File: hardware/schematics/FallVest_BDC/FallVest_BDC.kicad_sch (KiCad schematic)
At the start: 6 parts, among them Q1 AO3400A, U2 ESP32-WROOM-32, U3 4554, U4 NEO-6M

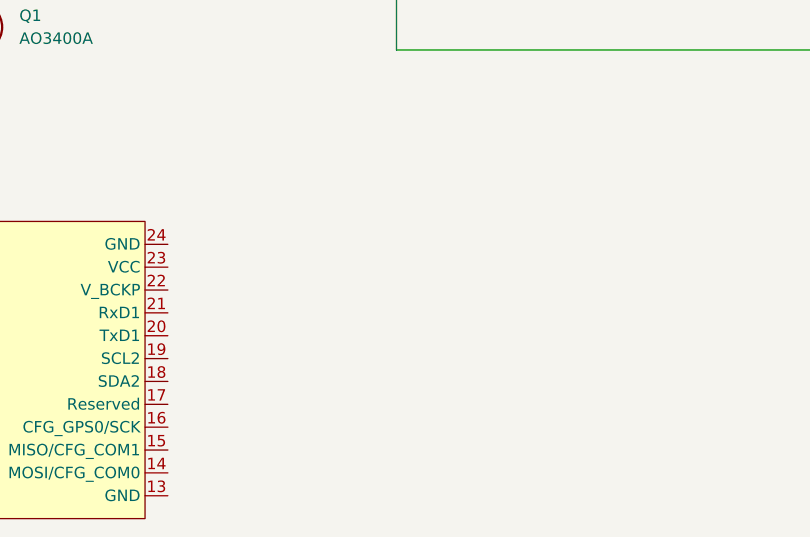
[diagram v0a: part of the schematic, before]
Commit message: Magnetometer
Added ICM-20948
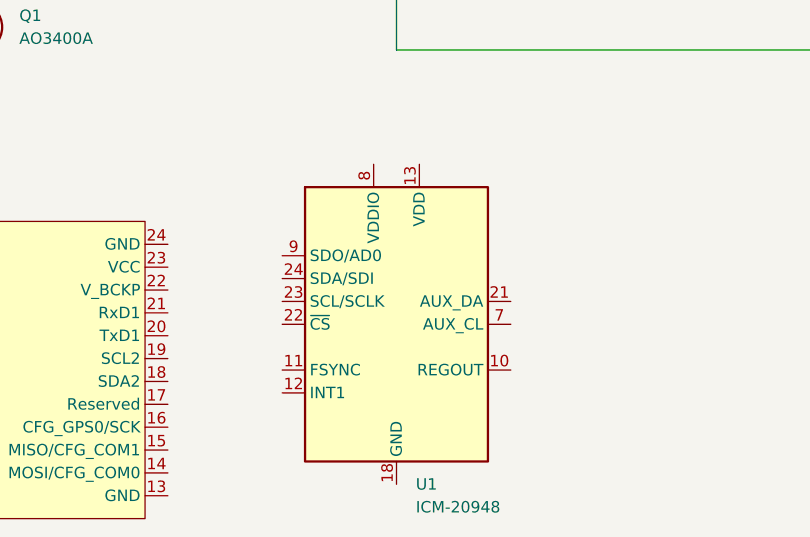
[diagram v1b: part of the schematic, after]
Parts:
- added U1: ICM-20948, Sensor_Motion:InvenSense_QFN-24_3x3mm_P0.4mm, symbol Sensor_Motion:ICM-20948
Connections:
- new net: U1.18 (GND), U1.20 (GND)
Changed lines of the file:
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@@
+	)
+	(symbol
+		(lib_id "Sensor_Motion:ICM-20948")
+		(at 88.9 168.91 0)
+		(unit 1)
+		(exclude_from_sim no)
+		(in_bom yes)
+		(on_board yes)
+		(dnp no)
+		(fields_autoplaced yes)
+		(property "Reference" "U1"
+			(at 91.0433 186.69 0)
+			(effects
+				(font
+					(size 1.27 1.27)
+				)
+				(justify left)
+			)
+		)
+		(property "Value" "ICM-20948"
+			(at 91.0433 189.23 0)
+			(effects
+				(font
+					(size 1.27 1.27)
+				)
+				(justify left)
+			)
+		)
+		(property "Footprint" "Sensor_Motion:InvenSense_QFN-24_3x3mm_P0.4mm"
+			(at 88.9 194.31 0)
+			(effects
+				(font
+					(size 1.27 1.27)
+				)
+				(hide yes)
+			)
+		)
+		(property "Datasheet" "http://www.invensense.com/wp-content/uploads/2016/06/DS-000189-ICM-20948-v1.3.pdf"
+			(at 88.9 172.72 0)
+			(effects
+				(font
+					(size 1.27 1.27)
+				)
+				(hide yes)
+			)
+		)
+		(property "Description" "InvenSense 9-Axis Motion Sensor, Accelerometer, Gyroscope, Compass, I2C/SPI, QFN-24"
+			(at 88.9 168.91 0)
+			(effects
+				(font
+					(size 1.27 1.27)
+				)
+				(hide yes)
+			)
+		)
+		(pin "13"
+		)
+		(pin "11"
+		)
+		(pin "20"
+		)
+		(pin "22"
+		)
+		(pin "9"
+		)
+		(pin "8"
+		)
+		(pin "6"
+		)
+		(pin "4"
+		)
+		(pin "1"
+		)
+		(pin "3"
+		)
+		(pin "2"
+		)
+		(pin "23"
+		)
+		(pin "12"
+		)
+		(pin "18"
+		)
+		(pin "5"
+		)
+		(pin "14"
+		)
+		(pin "15"
+		)
+		(pin "7"
+		)
+		(pin "10"
+		)
+		(pin "17"
+		)
+		(pin "24"
+		)
+		(pin "21"
+		)
+		(pin "16"
+		)
+		(pin "19"
+		)
+		(instances
+			(project ""
+				(path "/74063a4b-f2d6-40f5-8694-30dc3de3f53f"
+					(reference "U1")
+					(unit 1)
+				)
+			)
+		)
 	)
 	(symbol

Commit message: Update
Some minor tweaking.
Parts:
- removed U1: ICM-20948, Sensor_Motion:InvenSense_QFN-24_3x3mm_P0.4mm, symbol Sensor_Motion:ICM-20948
- added D1: SS34, Diode_SMD:D_SMA, symbol Diode:SS34
- added R: 220, symbol Device:R_US
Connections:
- net GND: now also Q1.2 (S), U2.1 (GND), U2.15 (GND), U2.38 (GND), U2.39 (GND); no longer U3.JP3_2 (SDO/ADR)
- net at Q1.1 (G): now also Q1.3 (D), D1.2 (A), R.2
- net at U4.20 (TxD1): now also U2.28 (IO17)
- net at U4.21 (RxD1): now also U2.27 (IO16)
- net at U3.JP3_1 (CS): now also U2.2 (VDD), U3.JP1_1 (VIN)
- net at U2.8 (IO32): now also R.1
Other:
- moved on the sheet: BT1, LS1, Q1, U2, U3A, U3B, U4

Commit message: Added SIM800L Core
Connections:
- net GND: now also U4.13 (GND)
- net at U4.23 (VCC): now also U2.2 (VDD), U3.JP1_1 (VIN), U3.JP3_1 (CS)
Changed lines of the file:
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@@
 	(paper "A4")
 	(junction
+		(at 124.46 113.03)
+		(diameter 0)
+		(color 0 0 0 0)
+	)
+	(junction
 		(at 129.54 101.6)
 		(diameter 0)
@@
 	)
 	(junction
+		(at 99.06 34.29)
+		(diameter 0)
+		(color 0 0 0 0)
+	)
+	(junction
 		(at 99.06 113.03)
 		(diameter 0)
@@
 	(wire
 		(pts
-			(xy 157.48 113.03) (xy 99.06 113.03)
+			(xy 99.06 26.67) (xy 99.06 34.29)
+		)
+		(stroke
+			(width 0)
+			(type default)
+		)
+	)
+	(wire
+		(pts
+			(xy 157.48 113.03) (xy 124.46 113.03)
 		)
 		(stroke
@@
 	(wire
 		(pts
+			(xy 124.46 59.69) (xy 121.92 59.69)
+		)
+		(stroke
+			(width 0)
+			(type default)
+		)
+	)
+	(wire
+		(pts
 			(xy 128.27 101.6) (xy 128.27 96.52)
 		)
@@
 	(wire
 		(pts
+			(xy 124.46 113.03) (xy 99.06 113.03)
+		)
+		(stroke
+			(width 0)
+			(type default)
+		)
+	)
+	(wire
+		(pts
 			(xy 149.86 106.68) (xy 129.54 106.68)
 		)
@@
 	(wire
 		(pts
+			(xy 121.92 59.69) (xy 121.92 26.67)
+		)
+		(stroke
+			(width 0)
+			(type default)
+		)
+	)
+	(wire
+		(pts
 			(xy 157.48 101.6) (xy 129.54 101.6)
 		)
@@
 	(wire
 		(pts
+			(xy 124.46 85.09) (xy 124.46 113.03)
+		)
+		(stroke
+			(width 0)
+			(type default)
+		)
+	)
+	(wire
+		(pts
 			(xy 44.45 29.21) (xy 72.39 29.21)
 		)
@@
 		)
 		(stroke
+			(width 0)
+			(type default)
+		)
+	)
+	(wire
+		(pts
+			(xy 121.92 26.67) (xy 99.06 26.67)
+		)
+		(stroke

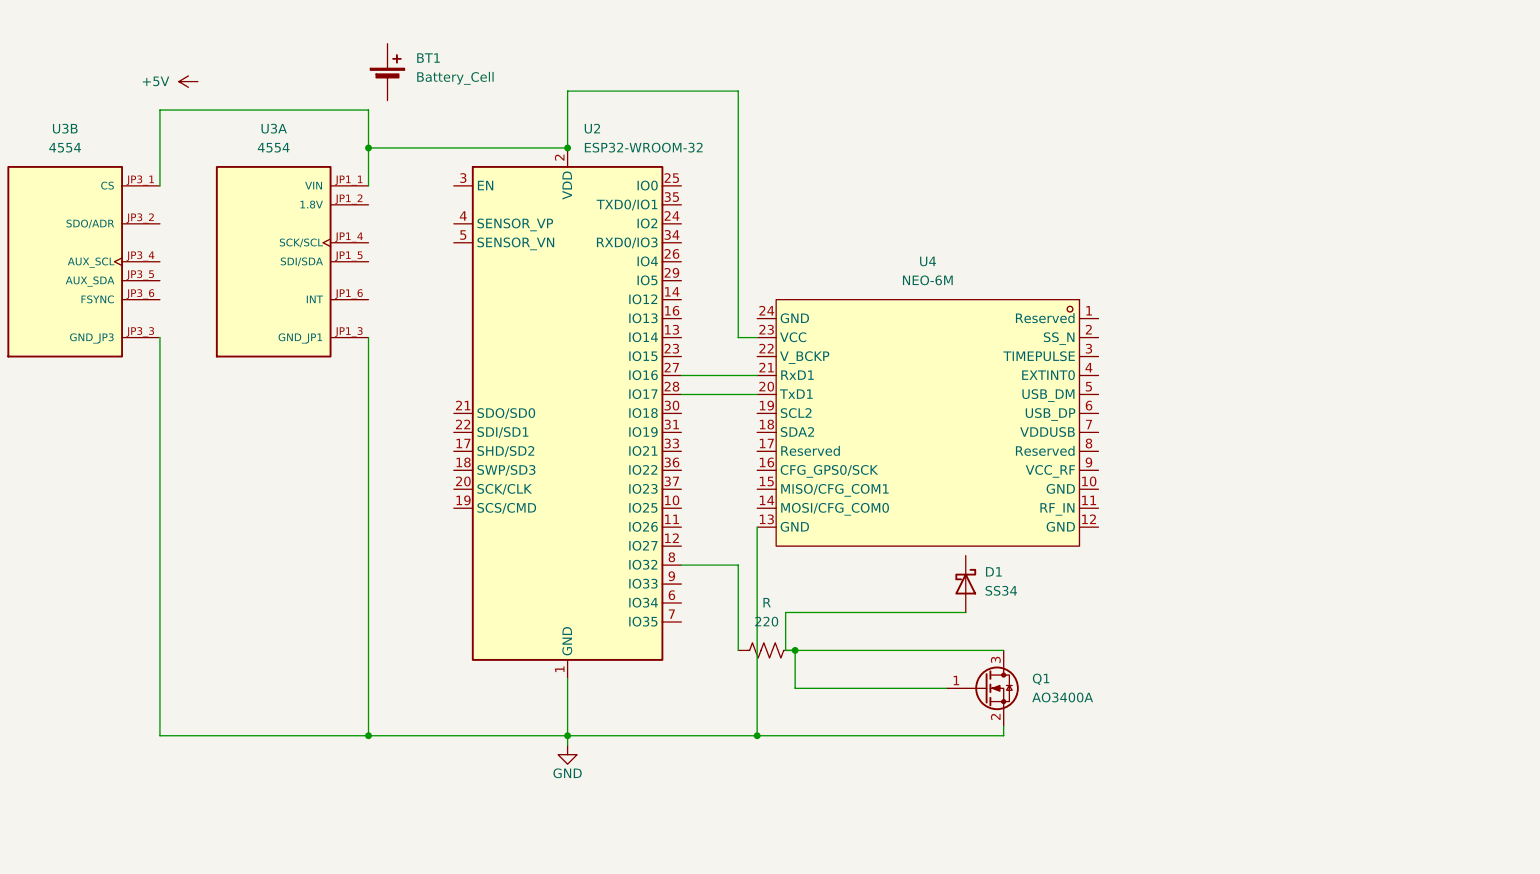
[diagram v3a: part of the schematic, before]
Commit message: Updated Schematic
SIM800L needed, having trouble with .sym
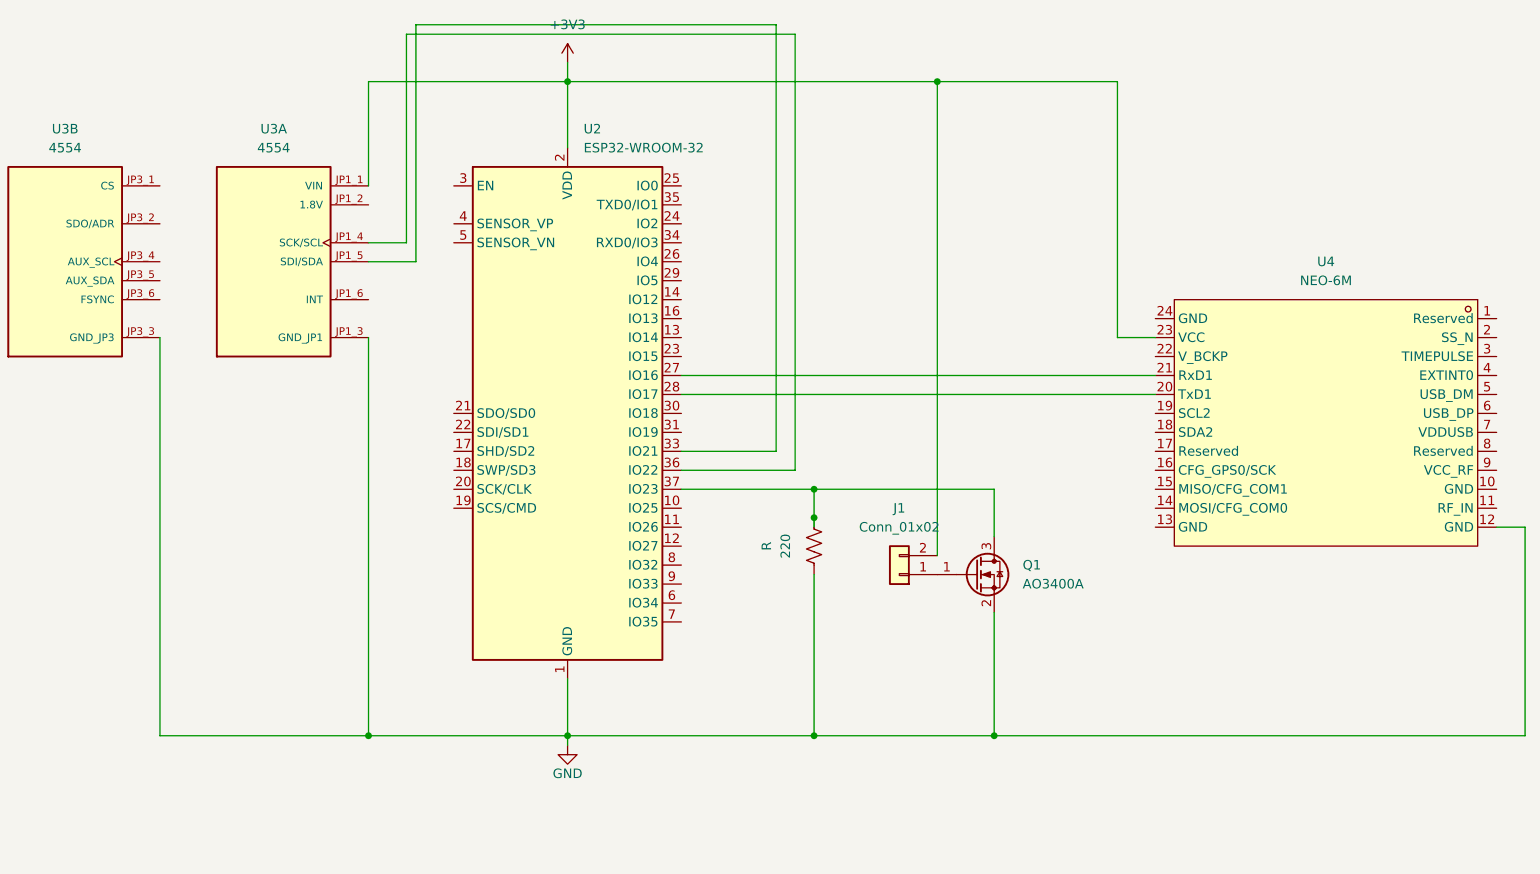
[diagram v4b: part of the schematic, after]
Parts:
- removed BT1: Battery_Cell, symbol Device:Battery_Cell
- removed D1: SS34, Diode_SMD:D_SMA, symbol Diode:SS34
- added J1: Conn_01x02, symbol Connector_Generic:Conn_01x02
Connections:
- net GND: now also R.1, U4.12 (GND); no longer U4.13 (GND)
- net at Q1.3 (D), R.2: now also U2.37 (IO23); no longer Q1.1 (G)
- net +3V3: now reaches U2.2 (VDD), U3.JP1_1 (VIN), U4.23 (VCC)
- net +3V3: now also J1.2 (Pin_2); no longer U3.JP3_1 (CS)
- net at U2.33 (IO21): now also U3.JP1_5 (SDI/SDA)
- net at U2.36 (IO22): now also U3.JP1_4 (SCK/SCL)
- net at U2.8 (IO32): no longer R.1
- new net: J1.1 (Pin_1), Q1.1 (G)
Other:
- moved on the sheet: Q1, R, U4

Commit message: All Parts
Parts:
- removed LS1: PS1420P02CT, PS1420P02CT_TDK, symbol 2026-09-14_03-29-42:PS1420P02CT
- added U1: SIM800L-CORE, symbol sim800l-core:SIM800L-CORE
- added U5: ICM-20948, Sensor_Motion:InvenSense_QFN-24_3x3mm_P0.4mm, symbol Sensor_Motion:ICM-20948
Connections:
- new net: U5.18 (GND), U5.20 (GND)
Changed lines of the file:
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@@
+	)
+	(symbol
+		(lib_id "Sensor_Motion:ICM-20948")
+		(at 55.88 147.32 0)
+		(unit 1)
+		(exclude_from_sim no)
+		(in_bom yes)
+		(on_board yes)
+		(dnp no)
+		(fields_autoplaced yes)
+		(property "Reference" "U5"
+			(at 58.0233 165.1 0)
+			(effects
+				(font
+					(size 1.27 1.27)
+				)
+				(justify left)
+			)
+		)
+		(property "Value" "ICM-20948"
+			(at 58.0233 167.64 0)
+			(effects
+				(font
+					(size 1.27 1.27)
+				)
+				(justify left)
+			)
+		)
+		(property "Footprint" "Sensor_Motion:InvenSense_QFN-24_3x3mm_P0.4mm"
+			(at 55.88 172.72 0)
+			(effects
+				(font
+					(size 1.27 1.27)
+				)
+				(hide yes)
+			)
+		)
+		(property "Datasheet" "http://www.invensense.com/wp-content/uploads/2016/06/DS-000189-ICM-20948-v1.3.pdf"
+			(at 55.88 151.13 0)
+			(effects
+				(font
+					(size 1.27 1.27)
+				)
+				(hide yes)
+			)
+		)
+		(property "Description" "InvenSense 9-Axis Motion Sensor, Accelerometer, Gyroscope, Compass, I2C/SPI, QFN-24"
+			(at 55.88 147.32 0)
+			(effects
+				(font
+					(size 1.27 1.27)
+				)
+				(hide yes)
+			)
+		)
+		(pin "2"
+		)
+		(pin "4"
+		)
+		(pin "24"
+		)
+		(pin "9"
+		)
+		(pin "23"
+		)
+		(pin "11"
+		)
+		(pin "22"
+		)
+		(pin "12"
+		)
+		(pin "1"
+		)
+		(pin "3"
+		)
+		(pin "5"
+		)
+		(pin "8"
+		)
+		(pin "18"
+		)
+		(pin "20"
+		)
+		(pin "13"
+		)
+		(pin "6"
+		)
+		(pin "17"
+		)
+		(pin "21"
+		)
+		(pin "7"
+		)
+		(pin "15"
+		)
+		(pin "16"
+		)
+		(pin "10"
+		)
+		(pin "19"
+		)
+		(pin "14"
+		)
+		(instances
+			(project ""
+				(path "/74063a4b-f2d6-40f5-8694-30dc3de3f53f"
+					(reference "U5")
+					(unit 1)
+				)
+			)
+		)
 	)
 	(symbol
@@
 	)
 	(symbol
-		(lib_id "2026-09-14_03-29-42:PS1420P02CT")
-		(at 180.34 148.59 180)
-		(unit 1)
-		(exclude_from_sim no)
-		(in_bom yes)
-		(on_board yes)
-		(dnp no)
-		(fields_autoplaced yes)
-		(property "Reference" "LS1"
-			(at 167.64 140.97 0)
-			(effects
-				(font
-					(size 1.524 1.524)
-				)
-			)
-		)
-		(property "Value" "PS1420P02CT"
-			(at 167.64 143.51 0)
-			(effects
-				(font
-					(size 1.524 1.524)
-				)
-			)
-		)
-		(property "Footprint" "PS1420P02CT_TDK"
-			(at 180.34 148.59 0)
-			(effects
-				(font
-					(size 1.27 1.27)
-					(italic yes)
-				)
-				(hide yes)
-			)
-		)
-		(property "Datasheet" "https://www.digikey.com/en/products/detail/adafruit-industries-llc/1536/26744063"
-			(at 180.34 148.59 0)
-			(effects
-				(font
-					(size 1.27 1.27)
-					(italic yes)
-				)
-				(hide yes)
-			)
-		)
-		(property "Description" "Buzzer"
-			(at 180.34 148.59 0)
-			(effects
-				(font
-					(size 1.27 1.27)
-				)
-				(hide yes)
-			)
-		)
-		(pin "1"
-		)
-		(pin "2"
-		)
-		(instances
-			(project ""
-				(path "/74063a4b-f2d6-40f5-8694-30dc3de3f53f"
-					(reference "LS1")
-					(unit 1)
-				)
-			)
-		)
-	)
-	(symbol
 		(lib_id "RF_Module:ESP32-WROOM-32")
 		(at 99.06 69.85 0)
@@
 					(unit 1)
 				)
+			)
+		)
+	)
+	(symbol
+		(lib_id "sim800l-core:SIM800L-CORE")
+		(at 242.57 31.75 0)
+		(unit 1)
+		(exclude_from_sim no)
+		(in_bom yes)
+		(on_board yes)
+		(dnp no)
+		(fields_autoplaced yes)
+		(property "Reference" "U1"
+			(at 243.205 19.05 0)
+			(effects
+				(font
+					(size 1.27 1.27)
+				)
+			)
+		)
+		(property "Value" "SIM800L-CORE"
+			(at 243.205 21.59 0)
+			(effects
+				(font
+					(size 1.27 1.27)
+				)
+			)
+		)
+		(property "Footprint" ""
+			(at 242.57 31.75 0)
+			(effects
+				(font
+					(size 1.27 1.27)
+				)
+				(hide yes)
+			)
+		)
+		(property "Datasheet" ""
+			(at 242.57 31.75 0)
+			(effects
+				(font
+					(size 1.27 1.27)
+				)
+				(hide yes)
+			)
+		)
+		(property "Description" ""
+			(at 242.57 31.75 0)
+			(effects
+				(font
+					(size 1.27 1.27)
+				)
+				(hide yes)
+			)
+		)
+		(pin "4"
+		)
+		(pin "10"
+		)
+		(pin "3"
+		)
+		(pin "9"
+		)
+		(pin "12"
+		)
+		(pin "1"
+		)
+		(pin "8"
+		)
+		(pin "11"
+		)
+		(pin "2"
+		)
+		(pin "7"
+		)
+		(pin "6"
+		)
+		(pin "5"
+		)
+		(instances
+			(project ""
+				(path "/74063a4b-f2d6-40f5-8694-30dc3de3f53f"
+					(reference "U1")
+					(unit 1)
+				)
